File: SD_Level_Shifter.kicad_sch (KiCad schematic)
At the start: 5 parts, among them U1 TXS0102QDCURQ1

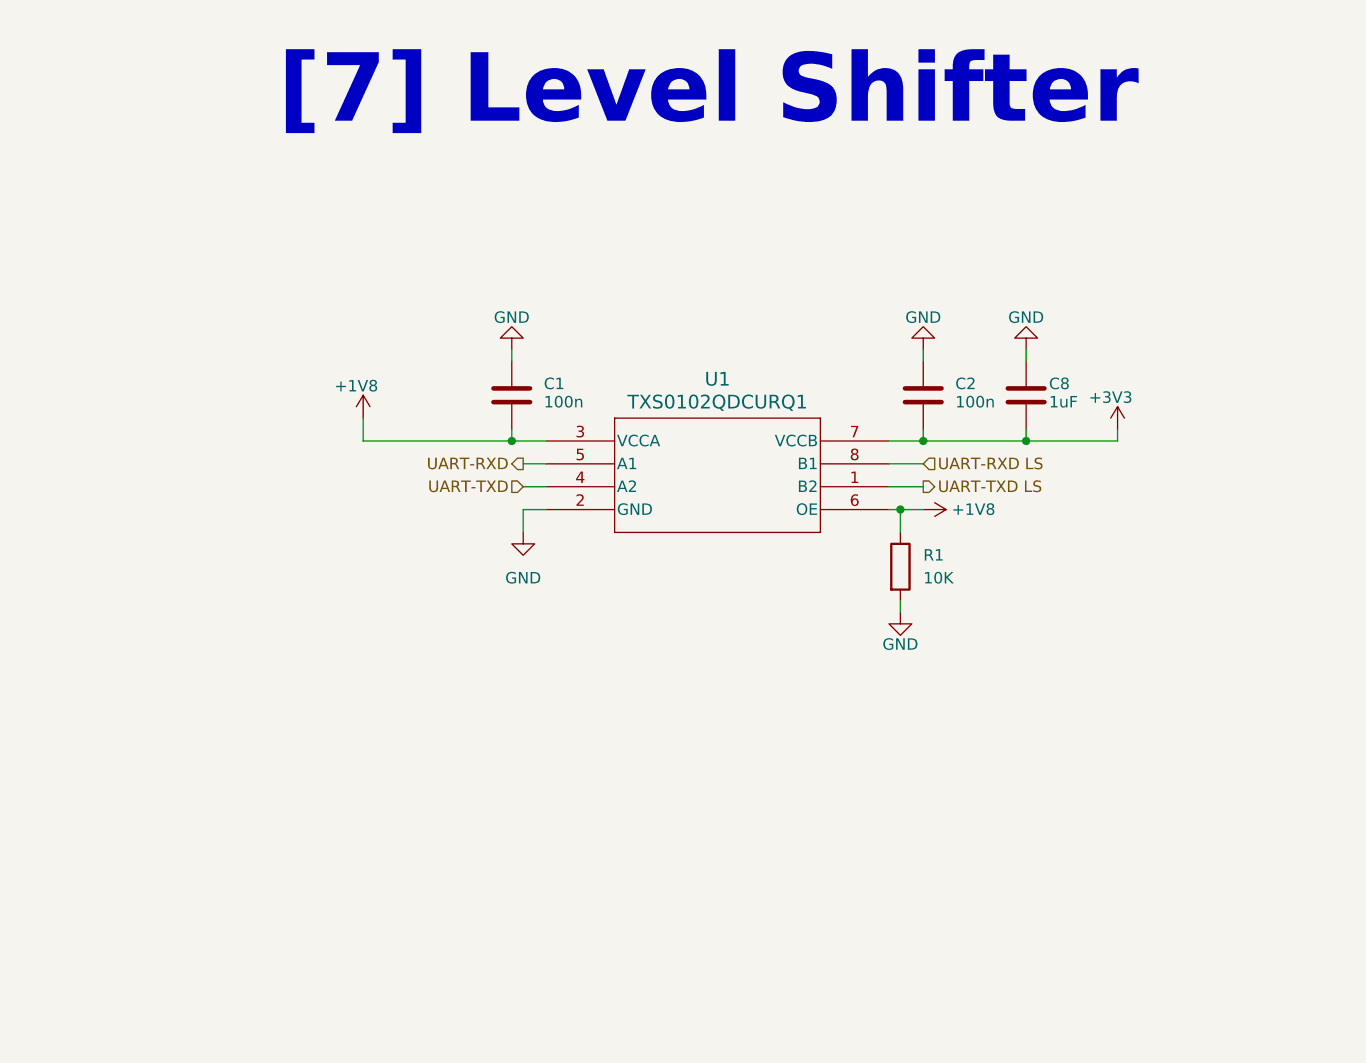
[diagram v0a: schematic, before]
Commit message: Added Level Shifter for SD card
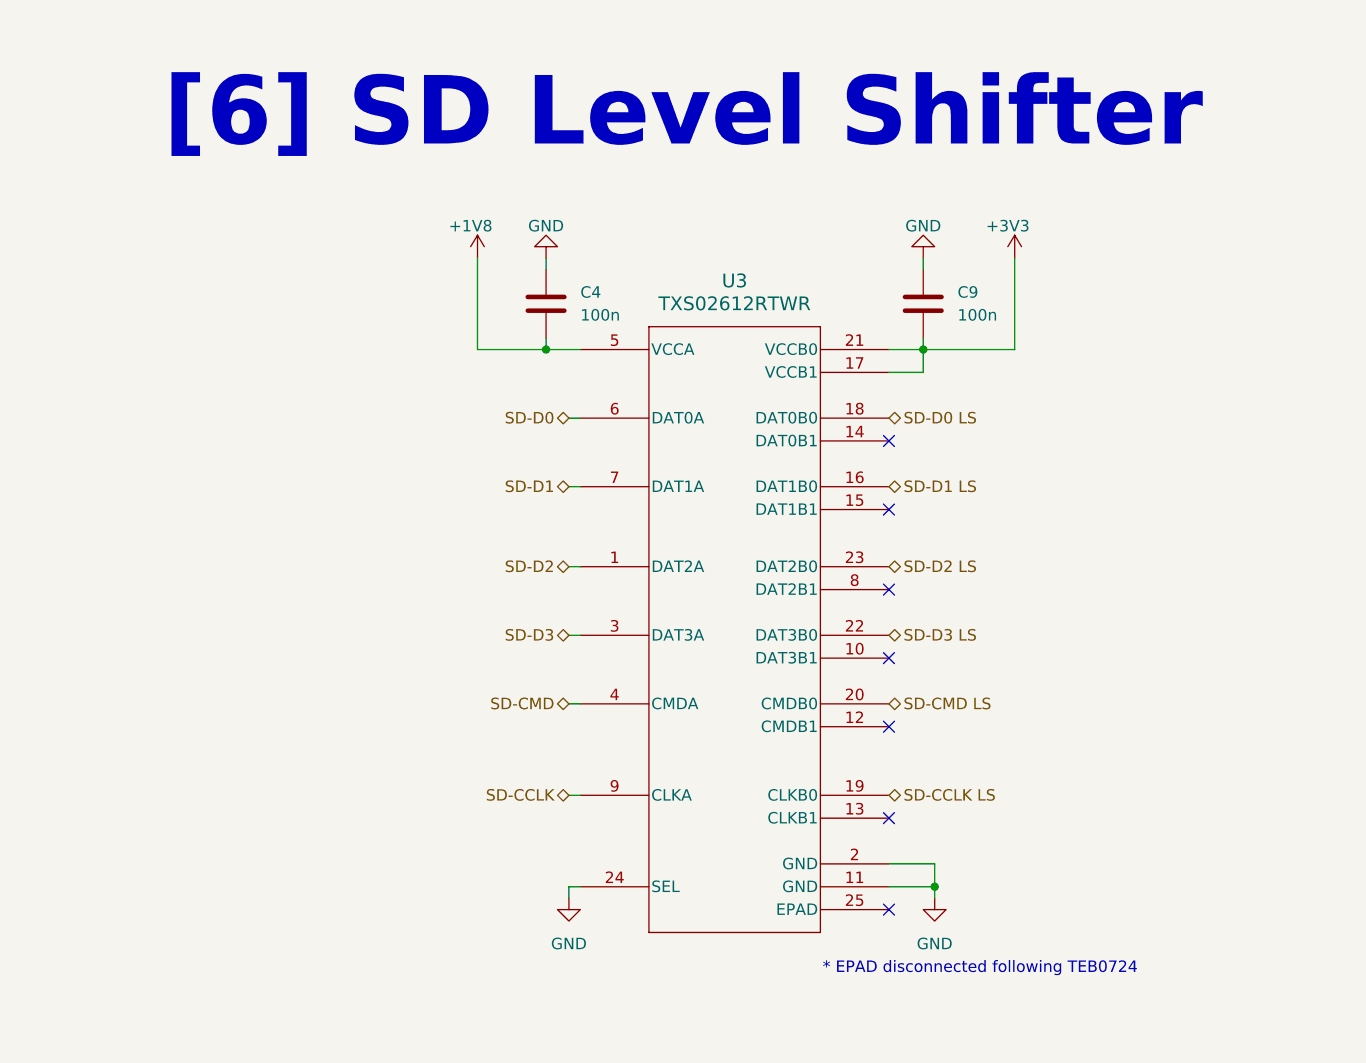
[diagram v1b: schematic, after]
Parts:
- removed C1, C2: 100n, Capacitor_SMD:C_0603_1608Metric, symbol Device:C
- removed C8: 1uF, Capacitor_SMD:C_0603_1608Metric, symbol Device:C
- removed R1: 10K, Resistor_SMD:R_0402_1005Metric, symbol Device:R
- removed U1: TXS0102QDCURQ1, adapter:TXS0102QDCURQ1, symbol adapter:TXS0102QDCURQ1
- added C4, C9: 100n, Capacitor_SMD:C_0603_1608Metric, symbol Device:C
- added U3: TXS02612RTWR, adapter:RTW24_2P45X2P45, symbol adapter:TXS02612RTWR
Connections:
- net +1V8: now also C4.2, U3.5 (VCCA)
- net +3V3: now also C9.2, U3.17 (VCCB1), U3.21 (VCCB0)
- net GND: now also C4.1, C9.1, U3.11 (GND), U3.2 (GND), U3.24 (SEL)
- new net SD-CCLK: U3.9 (CLKA)
- new net SD-CCLK LS: U3.19 (CLKB0)
- new net SD-CMD: U3.4 (CMDA)
- new net SD-CMD LS: U3.20 (CMDB0)
- new net SD-D0: U3.6 (DAT0A)
- new net SD-D0 LS: U3.18 (DAT0B0)
- new net SD-D1: U3.7 (DAT1A)
- new net SD-D1 LS: U3.16 (DAT1B0)
- new net SD-D2: U3.1 (DAT2A)
- new net SD-D2 LS: U3.23 (DAT2B0)
- new net SD-D3: U3.3 (DAT3A)
- new net SD-D3 LS: U3.22 (DAT3B0)
- no-connect marks 0 -> 7
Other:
- note added: "* EPAD disconnected following TEB0724"
- note added: "[6] SD Level Shifter"
- note removed: "[7] Level Shifter"

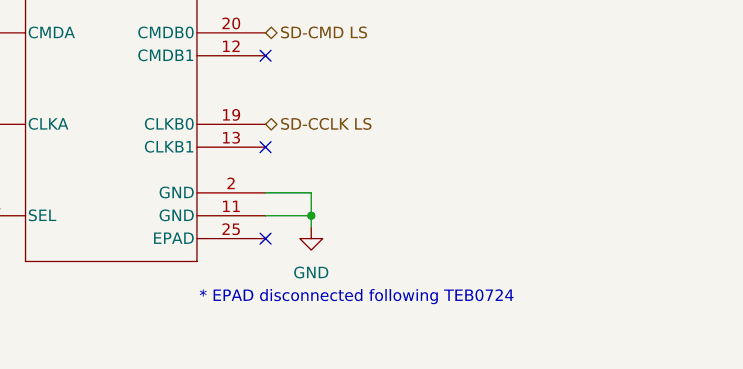
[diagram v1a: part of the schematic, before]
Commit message: Rerouted 3V3 trace
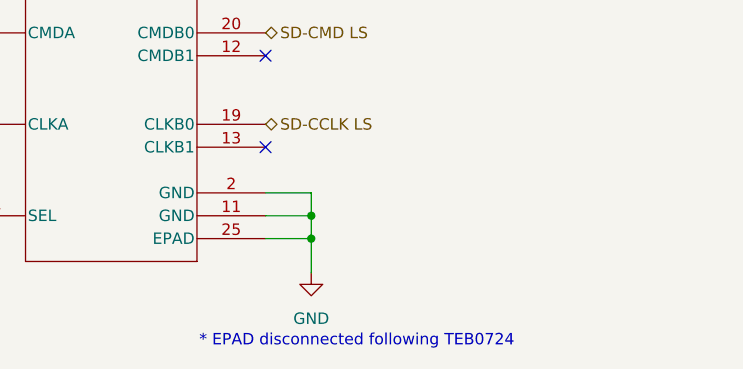
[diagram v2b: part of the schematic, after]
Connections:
- net GND: now also U3.25 (EPAD)
- no-connect marks 7 -> 6
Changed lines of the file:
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@@
 	(text "* EPAD disconnected following TEB0724"
 		(exclude_from_sim no)
-		(at 159.004 127.762 0)
+		(at 159.004 132.588 0)
 		(effects
 			(font
@@
 			(justify left top)
 		)
+	)
+	(junction
+		(at 171.45 121.92)
+		(diameter 0)
+		(color 0 0 0 0)
 	)
 	(junction
@@
 	)
 	(junction
+		(at 171.45 119.38)
+		(diameter 0)
+		(color 0 0 0 0)
+	)
+	(junction
 		(at 170.18 59.69)
 		(diameter 0)
 		(color 0 0 0 0)
 	)
-	(junction
-		(at 171.45 119.38)
-		(diameter 0)
-		(color 0 0 0 0)
-	)
 	(no_connect
 		(at 166.37 101.6)
@@
 	)
 	(no_connect
-		(at 166.37 121.92)
-	)
-	(no_connect
 		(at 166.37 86.36)
 	)
@@
 	(wire
 		(pts
+			(xy 171.45 121.92) (xy 171.45 125.73)
+		)
+		(stroke
+			(width 0)
+			(type default)
+		)
+	)
+	(wire
+		(pts
 			(xy 130.81 119.38) (xy 132.08 119.38)
 		)
@@
 	(wire
 		(pts
-			(xy 171.45 119.38) (xy 171.45 120.65)
+			(xy 171.45 119.38) (xy 171.45 121.92)
 		)
 		(stroke
@@
 		(pts
 			(xy 166.37 119.38) (xy 171.45 119.38)
+		)
+		(stroke
+			(width 0)
+			(type default)
+		)
+	)
+	(wire
+		(pts
+			(xy 166.37 121.92) (xy 171.45 121.92)
 		)
 		(stroke
@@
 	(symbol
 		(lib_id "power:GND")
-		(at 171.45 120.65 0)
+		(at 171.45 125.73 0)
 		(unit 1)
 		(body_style 1)
@@
 		(fields_autoplaced yes)
 		(property "Reference" "#PWR051"
-			(at 171.45 127 0)
+			(at 171.45 132.08 0)
 			(hide yes)
 			(show_name no)
@@
 		)
 		(property "Value" "GND"
+			(at 171.45 130.81 0)
+			(show_name no)
+			(do_not_autoplace no)
+			(effects
+				(font
+					(size 1.27 1.27)
+				)
+			)
+		)
+		(property "Footprint" ""
 			(at 171.45 125.73 0)
-			(show_name no)
-			(do_not_autoplace no)
-			(effects
-				(font
-					(size 1.27 1.27)
-				)
-			)
-		)
-		(property "Footprint" ""
-			(at 171.45 120.65 0)
 			(hide yes)
 			(show_name no)
@@
 		)
 		(property "Datasheet" ""
-			(at 171.45 120.65 0)
+			(at 171.45 125.73 0)
 			(hide yes)
 			(show_name no)
@@
 		)
 		(property "Description" "Power symbol creates a global label with name \"GND\" , ground"
-			(at 171.45 120.65 0)
-			(hide yes)
-			(show_name no)
+			(at 171.45 125.73 0)
+			(hide yes)
+			(show_name no)

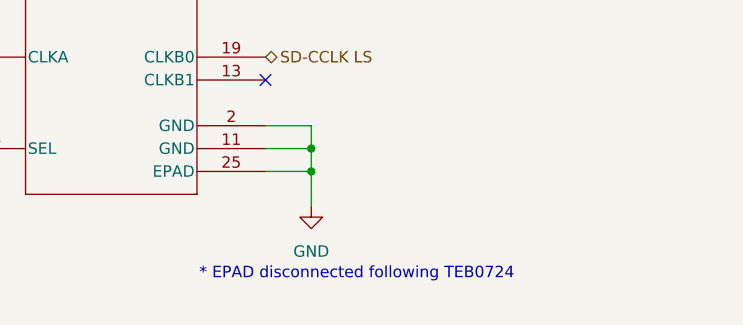
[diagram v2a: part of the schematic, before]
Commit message: Added pcb files for ethernet breakout board
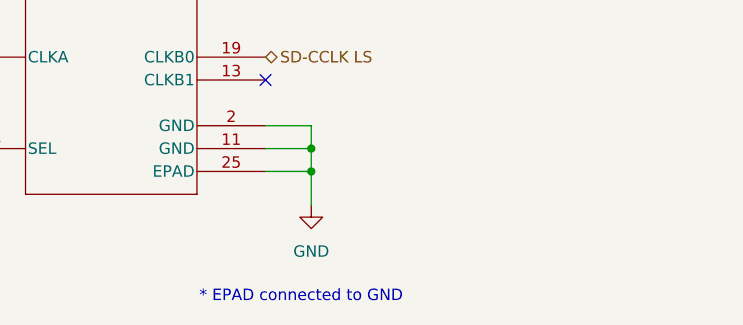
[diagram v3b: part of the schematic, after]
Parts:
- U3: External Part Number (none) -> 595-TXS02612RTWR; MPN (none) -> C140276
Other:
- note added: "* EPAD connected to GND"
- note removed: "* EPAD disconnected following TEB0724"
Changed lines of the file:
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@@
 		)
 	)
-	(text "* EPAD disconnected following TEB0724"
+	(text "* EPAD connected to GND"
 		(exclude_from_sim no)
-		(at 159.004 132.588 0)
+		(at 159.004 135.128 0)
 		(effects
 			(font
@@
 			)
 		)
+		(property "External Part Number" "595-TXS02612RTWR"
+			(at 113.03 62.23 0)
+			(hide yes)
+			(show_name no)
+			(do_not_autoplace no)
+			(effects
+				(font
+					(size 1.27 1.27)
+				)
+			)
+		)
+		(property "MPN" "C140276"
+			(at 113.03 62.23 0)
+			(hide yes)
+			(show_name no)
+			(do_not_autoplace no)
+			(effects
+				(font
+					(size 1.27 1.27)
+				)
+			)
+		)
 		(pin "22"
 		)
@@
 			)
 		)
+		(property "External Part Number" ""
+			(at 128.27 54.61 0)
+			(hide yes)
+			(show_name no)
+			(do_not_autoplace no)
+			(effects
+				(font
+					(size 1.27 1.27)
+				)
+			)
+		)
+		(property "MPN" ""
+			(at 128.27 54.61 0)
+			(hide yes)
+			(show_name no)
+			(do_not_autoplace no)
+			(effects
+				(font
+					(size 1.27 1.27)
+				)
+			)
+		)
 		(pin "1"
 		)
@@
 			(at 170.18 54.61 0)
 			(hide yes)
+			(show_name no)
+			(do_not_autoplace no)
+			(effects
+				(font
+					(size 1.27 1.27)
+				)
+			)
+		)
+		(property "External Part Number" ""
+			(at 170.18 54.61 0)
+			(hide yes)
+			(show_name no)
+			(do_not_autoplace no)
+			(effects
+				(font
+					(size 1.27 1.27)
+				)
+			)
+		)
+		(property "MPN" ""
+			(at 170.18 54.61 0)
+			(hide yes)

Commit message: Updated BOM and added fiducials
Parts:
- C4, C9: External Part Number (none) -> GCM188R71H104KA57J; MANUFACTURER (none) -> Murata Electronics; MPN (none) -> C3011652
- U3: External Part Number 595-TXS02612RTWR -> TXS02612RTWR; MANUFACTURER_PART_NUMBER TXS02612RTWR -> (none)
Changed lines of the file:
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@@
-			)
-		)
-		(property "MANUFACTURER_PART_NUMBER" "TXS02612RTWR"
-			(at 113.03 62.23 0)
-			(hide yes)
-			(show_name no)
-			(do_not_autoplace no)
-			(effects
-				(font
-					(size 1.27 1.27)
-				)
 			)
 		)
@@
 			)
 		)
-		(property "External Part Number" "595-TXS02612RTWR"
+		(property "External Part Number" "TXS02612RTWR"
 			(at 113.03 62.23 0)
 			(hide yes)
@@
 			)
 		)
-		(property "External Part Number" ""
+		(property "External Part Number" "GCM188R71H104KA57J"
 			(at 128.27 54.61 0)
 			(hide yes)
@@
 			)
 		)
-		(property "MPN" ""
+		(property "MPN" "C3011652"
+			(at 128.27 54.61 0)
+			(hide yes)
+			(show_name no)
+			(do_not_autoplace no)
+			(effects
+				(font
+					(size 1.27 1.27)
+				)
+			)
+		)
+		(property "MANUFACTURER" "Murata Electronics"
 			(at 128.27 54.61 0)
 			(hide yes)
@@
 			)
 		)
-		(property "External Part Number" ""
+		(property "External Part Number" "GCM188R71H104KA57J"
 			(at 170.18 54.61 0)
 			(hide yes)
@@
 			)
 		)
-		(property "MPN" ""
+		(property "MPN" "C3011652"
 			(at 170.18 54.61 0)
 			(hide yes)
+			(show_name no)
+			(do_not_autoplace no)
+			(effects
+				(font
+					(size 1.27 1.27)
+				)
+			)
+		)
+		(property "MANUFACTURER" "Murata Electronics"
+			(at 170.18 54.61 0)
+			(hide yes)

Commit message: added solder bridges and updated BOM
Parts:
- C4, C9: External Part Num (none) -> C3011652; External Part Number GCM188R71H104KA57J -> (none); MPN C3011652 -> GCM188R71H104KA57J
- U3: External Part Num (none) -> C140276; External Part Number TXS02612RTWR -> (none); MPN C140276 -> TXS02612RTWR
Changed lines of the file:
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@@
 			)
 		)
-		(property "External Part Number" "TXS02612RTWR"
+		(property "MPN" "TXS02612RTWR"
 			(at 113.03 62.23 0)
 			(hide yes)
@@
 			)
 		)
-		(property "MPN" "C140276"
+		(property "External Part Num" "C140276"
 			(at 113.03 62.23 0)
 			(hide yes)
@@
 			)
 		)
-		(property "External Part Number" "GCM188R71H104KA57J"
+		(property "MPN" "GCM188R71H104KA57J"
 			(at 128.27 54.61 0)
 			(hide yes)
@@
 			)
 		)
-		(property "MPN" "C3011652"
+		(property "MANUFACTURER" "Murata Electronics"
 			(at 128.27 54.61 0)
 			(hide yes)
@@
 			)
 		)
-		(property "MANUFACTURER" "Murata Electronics"
+		(property "External Part Num" "C3011652"
 			(at 128.27 54.61 0)
 			(hide yes)
@@
 			)
 		)
-		(property "External Part Number" "GCM188R71H104KA57J"
-			(at 170.18 54.61 0)
-			(hide yes)
-			(show_name no)
-			(do_not_autoplace no)
-			(effects
-				(font
-					(size 1.27 1.27)
-				)
-			)
-		)
-		(property "MPN" "C3011652"
+		(property "MPN" "GCM188R71H104KA57J"
 			(at 170.18 54.61 0)
 			(hide yes)
@@
 			(at 170.18 54.61 0)
 			(hide yes)
+			(show_name no)
+			(do_not_autoplace no)
+			(effects
+				(font
+					(size 1.27 1.27)
+				)
+			)
+		)
+		(property "External Part Num" "C3011652"
+			(at 170.18 54.61 0)
+			(hide yes)
